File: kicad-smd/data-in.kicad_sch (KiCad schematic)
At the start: 37 parts, among them SW0 SW_SPDT, SW1 SW_SPDT, SW2 SW_SPDT, SW3 SW_SPDT, SW4 SW_SPDT, SW5 SW_SPDT, SW6 SW_SPDT, SW7 SW_SPDT, SW8 SW_SPDT, SW9 SW_SPDT

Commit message: file updates
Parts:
- removed JP1: Jumper, Connector_PinHeader_2.54mm:PinHeader_1x02_P2.54mm_Vertical, symbol Jumper:Jumper_2_Bridged
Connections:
- net VIO_2V5: now also SW0.3 (C), SW1.3 (C), SW2.3 (C), SW3.3 (C), SW4.3 (C), SW5.3 (C), SW6.3 (C), SW7.3 (C), SW8.3 (C), SW9.3 (C)
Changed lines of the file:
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@@
-    (stroke (width 0) (type default) (color 0 0 0 0))
-  )
-  (wire (pts (xy 163.83 38.1) (xy 171.45 38.1))
     (stroke (width 0) (type default) (color 0 0 0 0))
   )
@@
     (stroke (width 0) (type default) (color 0 0 0 0))
   )
-  (wire (pts (xy 149.86 38.1) (xy 153.67 38.1))
+  (wire (pts (xy 160.02 38.1) (xy 171.45 38.1))
     (stroke (width 0) (type default) (color 0 0 0 0))
   )
@@
     )
   )
-  (global_label "VIO_2V5" (shape input) (at 149.86 38.1 180) (fields_autoplaced)
-    (effects (font (size 1.27 1.27)) (justify right))
-    (property "Intersheet References" "${INTERSHEET_REFS}" (id 0) (at 139.9479 38.0206 0)
+  (global_label "VIO_2V5" (shape input) (at 160.02 38.1 180) (fields_autoplaced)
+    (effects (font (size 1.27 1.27)) (justify right))
+    (property "Intersheet References" "${INTERSHEET_REFS}" (id 0) (at 150.1079 38.0206 0)
       (effects (font (size 1.27 1.27)) (justify right) hide)
     )
@@
     (pin "3")
   )
-  (symbol (lib_id "Jumper:Jumper_2_Bridged") (at 158.75 38.1 180) (unit 1)
-    (in_bom yes) (on_board yes)
-    (property "Reference" "JP1" (id 0) (at 157.48 35.56 0)
-      (effects (font (size 1.27 1.27)) (justify right))
-    )
-    (property "Value" "Jumper" (id 1) (at 154.94 41.91 0)
-      (effects (font (size 1.27 1.27)) (justify right))
-    )
-    (property "Footprint" "Connector_PinHeader_2.54mm:PinHeader_1x02_P2.54mm_Vertical" (id 2) (at 158.75 38.1 0)
-      (effects (font (size 1.27 1.27)) hide)
-    )
-    (property "Datasheet" "~" (id 3) (at 158.75 38.1 0)
-      (effects (font (size 1.27 1.27)) hide)
-    )
-    (pin "1")
-    (pin "2")
-  )
   (symbol (lib_id "Device:R_Small") (at 189.23 66.04 180) (unit 1)

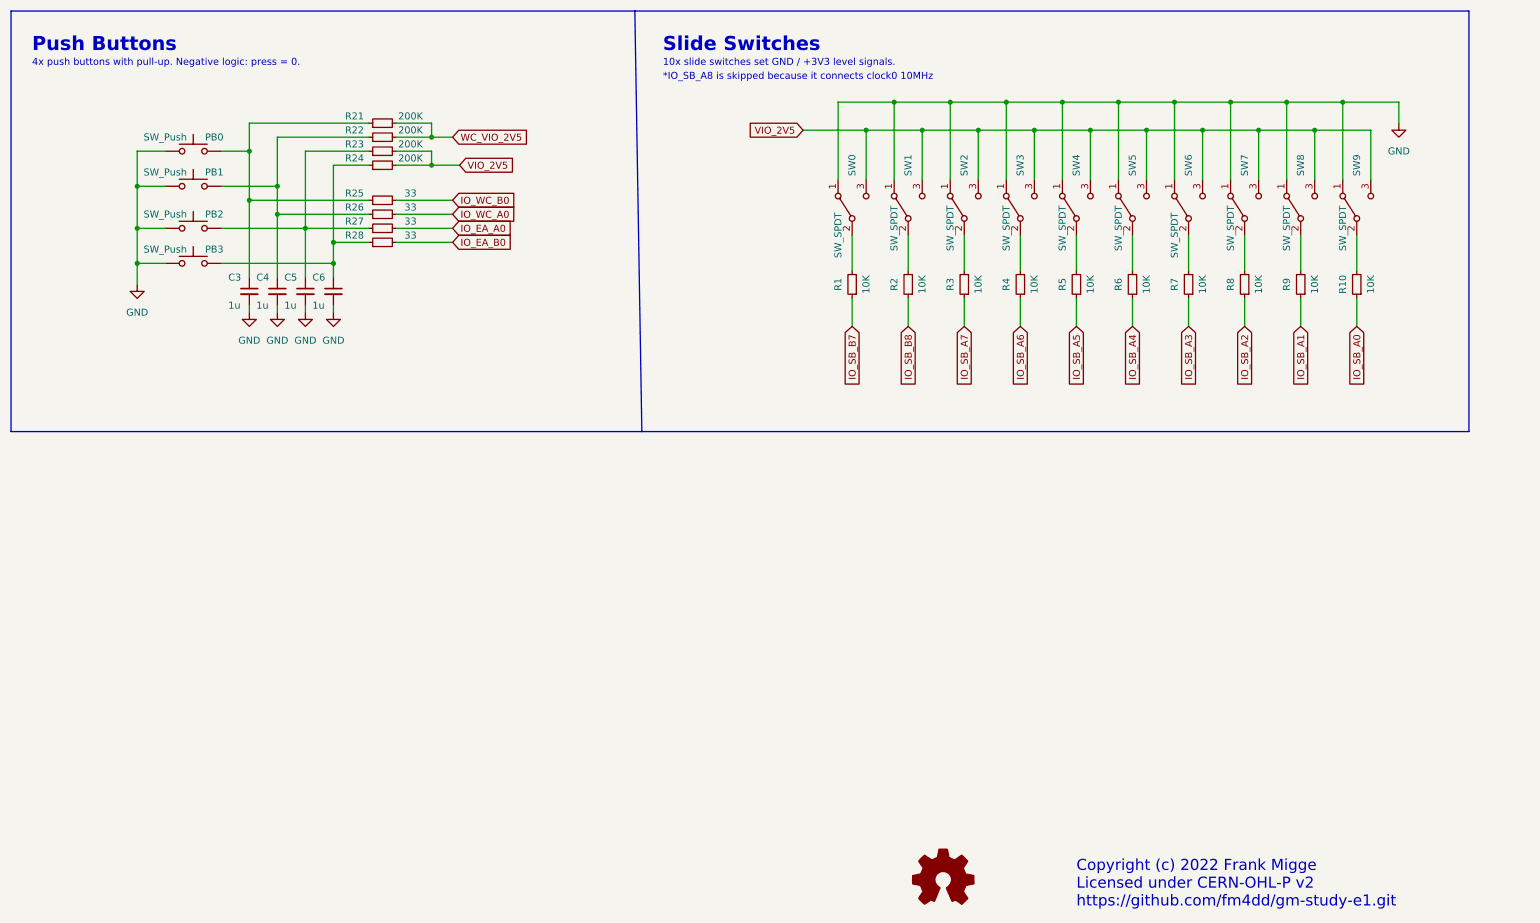
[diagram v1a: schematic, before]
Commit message: New SMB PCB v1.1 updates J1 level translation IC
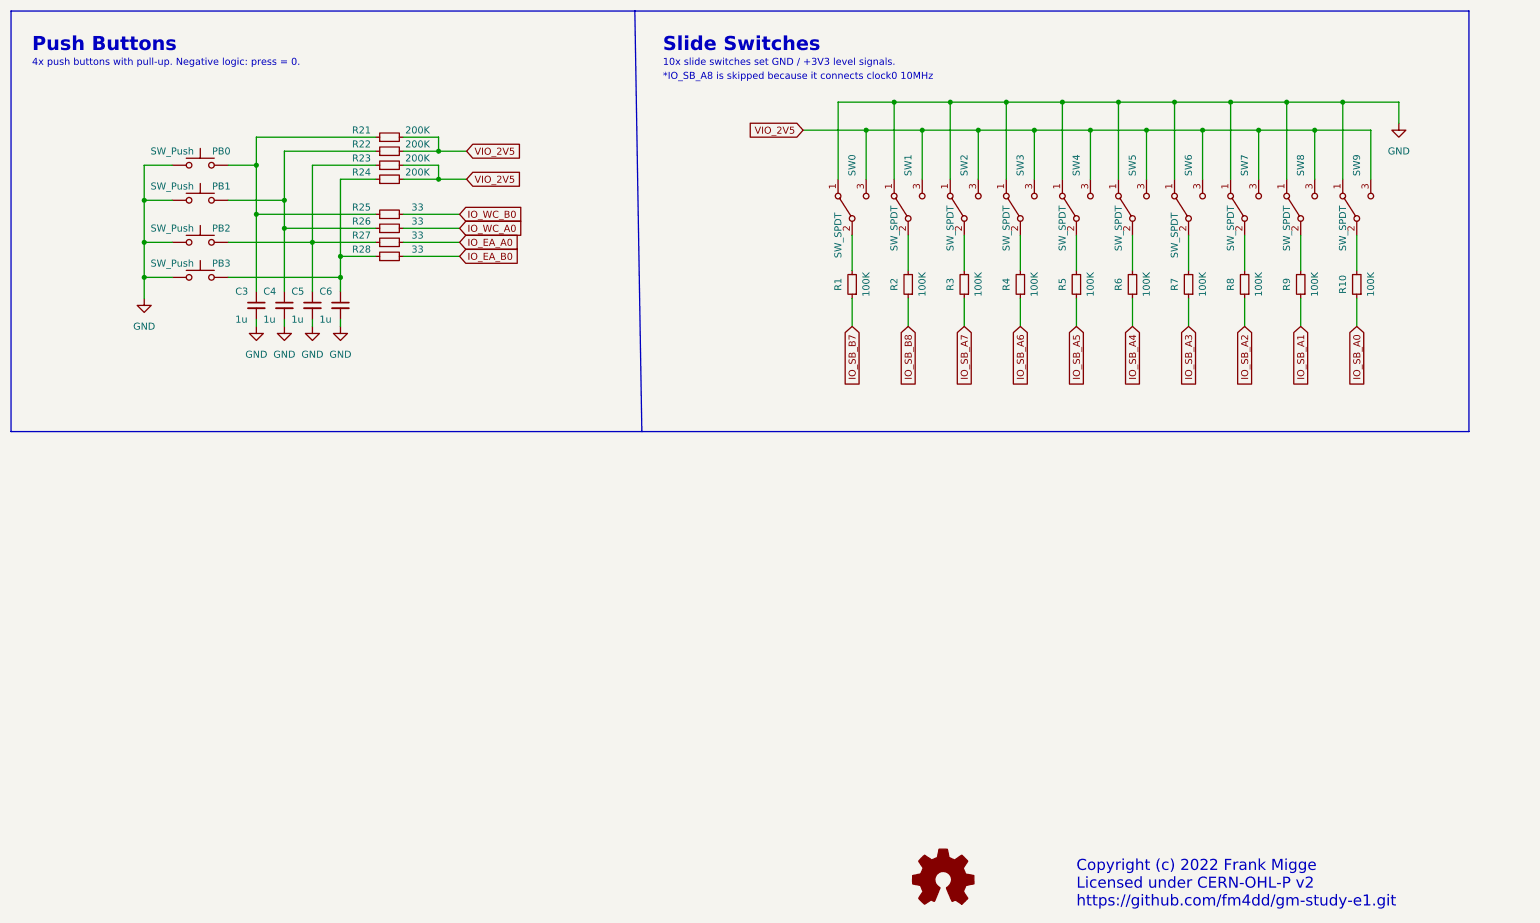
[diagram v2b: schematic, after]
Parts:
- R1, R10, R2, R3, R4, R5, R6, R7, R8, R9: value 10K -> 100K
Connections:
- net WC_VIO_2V5 is gone; now on net VIO_2V5: R21.2, R22.2
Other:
- moved on the sheet: C3, C4, C5, C6, PB0, PB1, PB2, PB3, R21, R22, R23, R24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
